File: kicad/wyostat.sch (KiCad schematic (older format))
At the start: 78 parts, among them J1 24 V AC IN, J13 USB_microAB, J16 5V_SEL, J2 OUT1, J3 OUT2, J4 OUT3, J5 I2C_ext1, Q1 BT136-600, Q2 BT136-600, Q3 BT136-600, U1 MOC3063M, U2 MOC3063M, U3 MOC3063M, U4 Wemos-Lolin, U5 MAX17502FATB+T

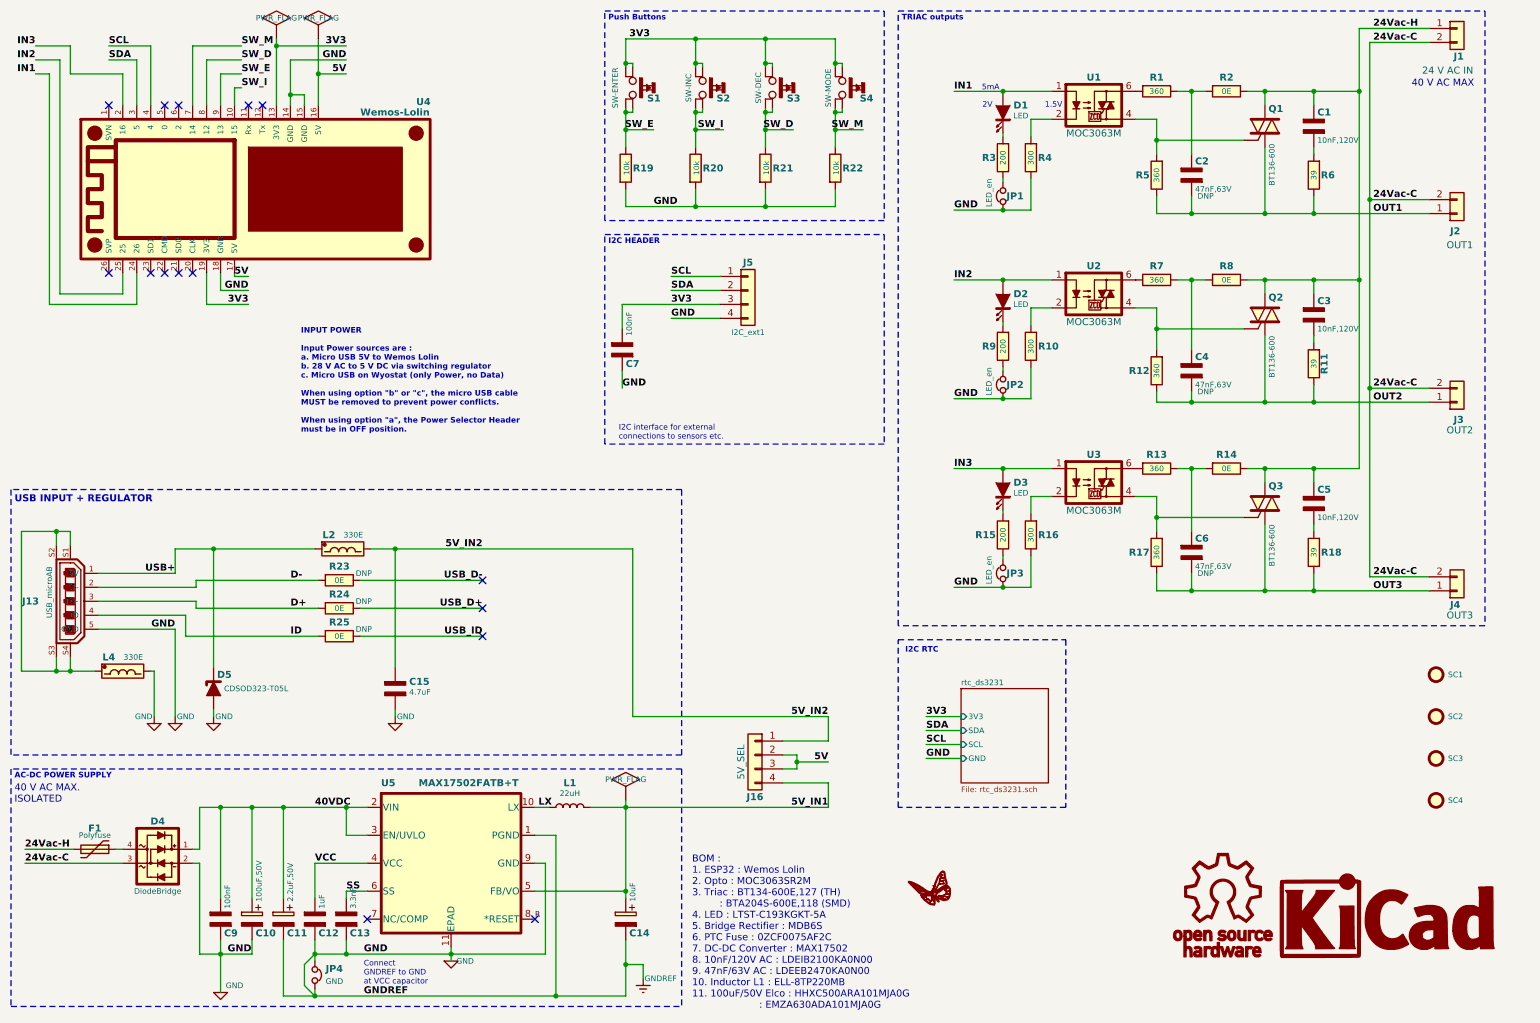
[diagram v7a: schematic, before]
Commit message: Gerbers ready for OSHpark
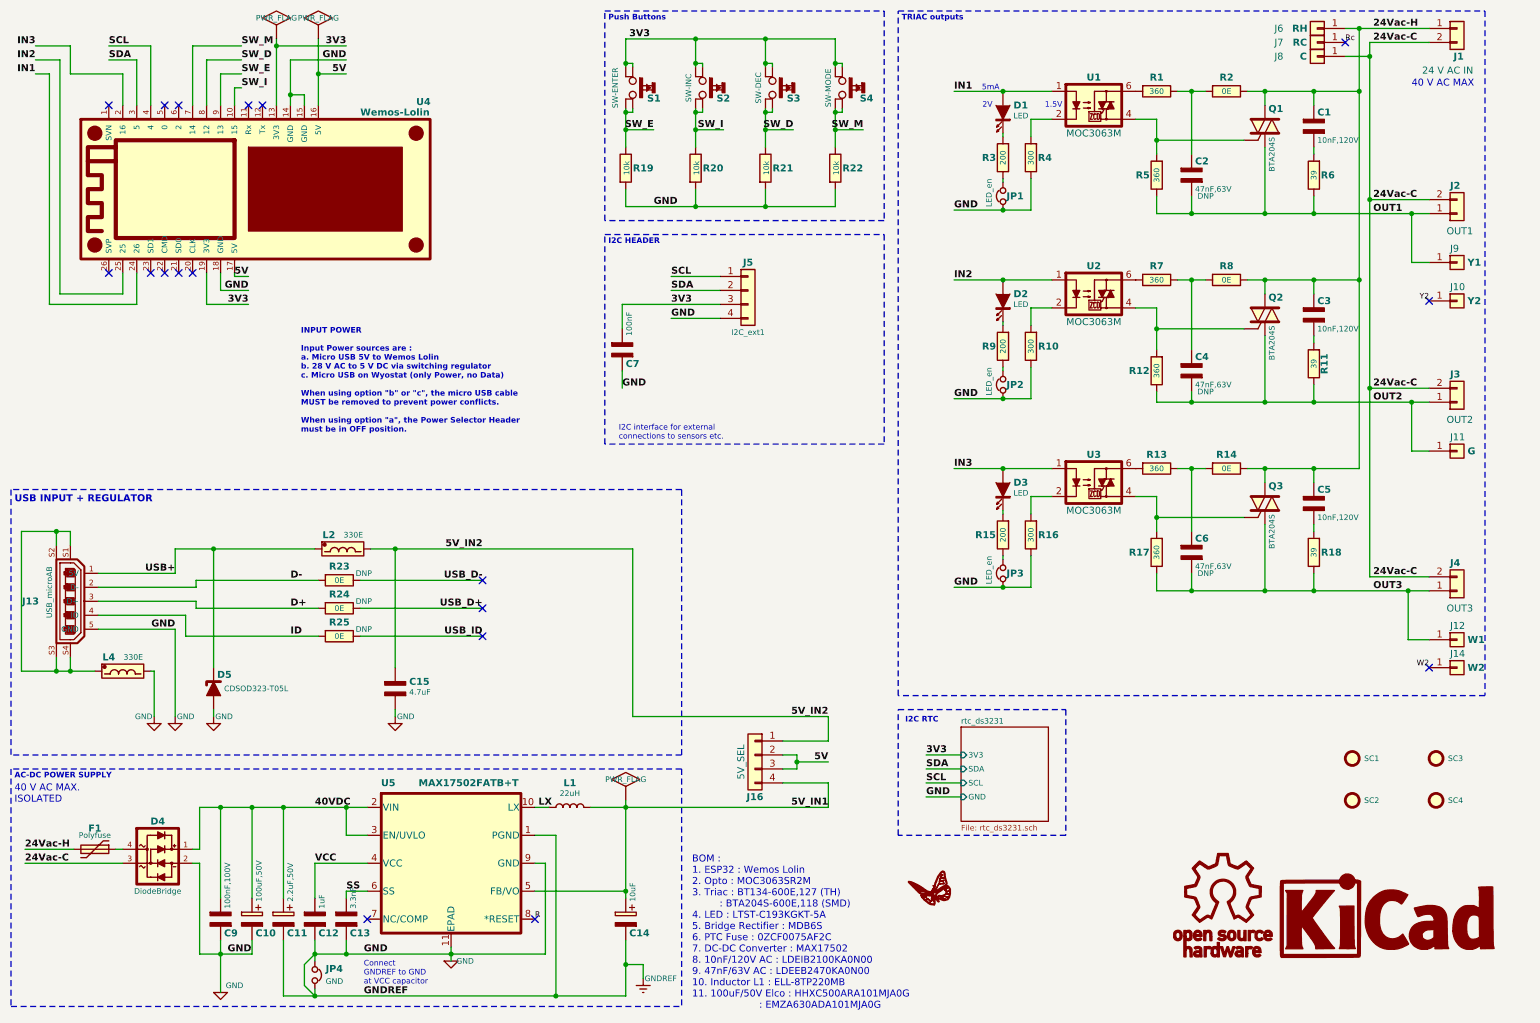
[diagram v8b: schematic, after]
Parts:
- added J10: Y2, wyostat_fp:pad_rect_smd, symbol wyostat:Conn_01x01
- added J11: G, wyostat_fp:pad_rect_smd, symbol wyostat:Conn_01x01
- added J12: W1, wyostat_fp:pad_rect_smd, symbol wyostat:Conn_01x01
- added J14: W2, wyostat_fp:pad_rect_smd, symbol wyostat:Conn_01x01
- added J6: RH, wyostat_fp:pad_rect_smd, symbol wyostat:Conn_01x01
- added J7: RC, wyostat_fp:pad_rect_smd, symbol wyostat:Conn_01x01
- added J8: C, wyostat_fp:pad_rect_smd, symbol wyostat:Conn_01x01
- added J9: Y1, wyostat_fp:pad_rect_smd, symbol wyostat:Conn_01x01
- C1, C2, C3, C4, C5, C6: footprint wyostat_fp:C_2220 -> wyostat_fp:C_1210
- C9: value 100nF -> 100nF,100V; manf# (none) -> mfr_pn
- Q1, Q2, Q3: value BT136-600 -> BTA204S
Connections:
- net 24Vac-C: now also J8.1 (Pin_1)
- net 24Vac-H: now also J6.1 (Pin_1)
- net OUT1: now also J9.1 (Pin_1)
- net OUT2: now also J11.1 (Pin_1)
- net OUT3: now also J12.1 (Pin_1)
- new net Rc: J7.1 (Pin_1)
- new net W2: J14.1 (Pin_1)
- new net Y2: J10.1 (Pin_1)
- no-connect marks 15 -> 18
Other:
- moved on the sheet: SC1, SC2
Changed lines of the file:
@@
 P 9550 1400
 F 0 "Q1" H 9575 1525 50  0000 L CNB
-F 1 "BT136-600" V 9600 975 40  0000 L CNN
+F 1 "BTA204S" V 9600 1075 40  0000 L CNN
 F 2 "wyostat_fp:DPAK-2" H 9750 1325 50  0001 L CIN
 F 3 "" H 9550 1400 50  0000 L CNN
@@
 F 0 "C2" H 9050 1850 50  0000 L CNB
 F 1 "47nF,63V" H 9050 1650 40  0000 L CNN
-F 2 "wyostat_fp:C_2220" H 9025 1750 60  0001 C CNN
+F 2 "wyostat_fp:C_1210" H 9025 1750 60  0001 C CNN
 F 3 "" H 9025 1750 60  0000 C CNN
 F 4 "Value" H 9025 1750 50  0001 C CNN "manf#"
@@
 U 1 1 5AA726AC
 P 10925 2025
-F 0 "J2" H 10875 2150 50  0000 L CNB
-F 1 "OUT1" H 10850 2250 50  0000 L CNN
+F 0 "J2" H 10875 1825 50  0000 L CNB
+F 1 "OUT1" H 10850 2150 50  0000 L CNN
 F 2 "wyostat_fp:TerminalBlock_Pheonix_MPT-2.54mm_2pol" H 10925 2025 50  0001 C CNN
 F 3 "~" H 10925 2025 50  0001 C CNN
@@
 P 9550 2750
 F 0 "Q2" H 9575 2875 50  0000 L CNB
-F 1 "BT136-600" V 9600 2300 40  0000 L CNN
+F 1 "BTA204S" V 9600 2425 40  0000 L CNN
 F 2 "wyostat_fp:DPAK-2" H 9750 2675 50  0001 L CIN
 F 3 "" H 9550 2750 50  0000 L CNN
@@
 U 1 1 5AA791CF
 P 10925 3375
-F 0 "J3" H 10900 3500 50  0000 L CNB
-F 1 "OUT2" H 10850 3575 50  0000 L CNN
+F 0 "J3" H 10875 3175 50  0000 L CNB
+F 1 "OUT2" H 10850 3500 50  0000 L CNN
 F 2 "wyostat_fp:TerminalBlock_Pheonix_MPT-2.54mm_2pol" H 10925 3375 50  0001 C CNN
 F 3 "~" H 10925 3375 50  0001 C CNN
@@
 P 9550 4100
 F 0 "Q3" H 9575 4225 50  0000 L CNB
-F 1 "BT136-600" V 9600 3650 40  0000 L CNN
+F 1 "BTA204S" V 9600 3775 40  0000 L CNN
 F 2 "wyostat_fp:DPAK-2" H 9750 4025 50  0001 L CIN
 F 3 "" H 9550 4100 50  0000 L CNN
@@
 U 1 1 5AA7ACF2
 P 10925 4725
-F 0 "J4" H 10875 4825 50  0000 L CNB
-F 1 "OUT3" H 10850 4900 50  0000 L CNN
+F 0 "J4" H 10875 4525 50  0000 L CNB
+F 1 "OUT3" H 10850 4850 50  0000 L CNN
 F 2 "wyostat_fp:TerminalBlock_Pheonix_MPT-2.54mm_2pol" H 10925 4725 50  0001 C CNN
 F 3 "~" H 10925 4725 50  0001 C CNN
@@
 	6925 575  11125 575
 Wire Notes Line
-	11125 4975 6925 4975
+	11125 5475 6925 5475
 Text Notes 6950 650  0    40   ~ 8
 TRIAC outputs
@@
 P 2075 7075
 F 0 "C9" H 2100 6975 50  0000 L CNB
-F 1 "100nF" V 2125 7150 40  0000 L CNN
+F 1 "100nF,100V" V 2125 7150 40  0000 L CNN
 F 2 "wyostat_fp:C_0805" H 2075 7075 60  0001 C CNN
 F 3 "" H 2075 7075 60  0000 C CNN
+F 4 "mfr_pn" H 2075 7075 50  0001 C CNN "manf#"
 	1    2075 7075
 	1    0    0    -1
@@
 F 0 "C1" H 9925 1500 50  0000 L CNB
 F 1 "10nF,120V" H 9925 1300 40  0000 L CNN
-F 2 "wyostat_fp:C_2220" H 9900 1400 60  0001 C CNN
+F 2 "wyostat_fp:C_1210" H 9900 1400 60  0001 C CNN
 F 3 "" H 9900 1400 60  0000 C CNN
 	1    9900 1400
@@
 F 0 "C3" H 9925 2850 50  0000 L CNB
 F 1 "10nF,120V" H 9925 2650 40  0000 L CNN
-F 2 "wyostat_fp:C_2220" H 9900 2750 60  0001 C CNN
+F 2 "wyostat_fp:C_1210" H 9900 2750 60  0001 C CNN
 F 3 "" H 9900 2750 60  0000 C CNN
 	1    9900 2750
@@
 F 0 "C5" H 9925 4200 50  0000 L CNB
 F 1 "10nF,120V" H 9925 4000 40  0000 L CNN
-F 2 "wyostat_fp:C_2220" H 9900 4100 60  0001 C CNN
+F 2 "wyostat_fp:C_1210" H 9900 4100 60  0001 C CNN
 F 3 "" H 9900 4100 60  0000 C CNN
 	1    9900 4100
@@
 $EndComp
 Wire Notes Line
-	11125 575  11125 4975
+	11125 575  11125 5475
 Wire Notes Line
-	6925 4975 6925 575
+	6925 5475 6925 575
 Wire Wire Line
 	3725 7325 2975 7325
@@
 	10725 700  10225 700
 Wire Wire Line
-	10300 800  10300 1925
+	10300 800  10300 900
 Wire Wire Line
 	10300 800  10725 800
@@
 Connection ~ 10300 3275
 Wire Wire Line
-	9900 2025 10725 2025
+	9900 2025 10600 2025
 Wire Wire Line
-	9900 3375 10725 3375
+	9900 3375 10600 3375
 Wire Wire Line
-	9900 4725 10725 4725
+	9900 4725 10575 4725
 Wire Wire Line
 	9900 1150 10225 1150
@@
 L wyostat:SCREW SC1
 U 1 1 5AED1CEA
-P 10775 5325
-F 0 "SC1" H 10860 5325 40  0000 L CNN
-F 1 "SCREW" H 10775 5425 40  0001 C CNN
-F 2 "wyostat_fp:MountingHole_3.2mm_M3_Pad_Via" H 10775 5325 60  0001 C CNN
-F 3 "" H 10775 5325 60  0000 C CNN
-	1    10775 5325
+P 10175 5925
+F 0 "SC1" H 10260 5925 40  0000 L CNN
+F 1 "SCREW" H 10175 6025 40  0001 C CNN
+F 2 "wyostat_fp:MountingHole_3.2mm_M3_Pad_Via" H 10175 5925 60  0001 C CNN
+F 3 "" H 10175 5925 60  0000 C CNN
+	1    10175 5925
 	1    0    0    -1
 $EndComp
@@
 L wyostat:SCREW SC2
 U 1 1 5AED2014
-P 10775 5625
-F 0 "SC2" H 10860 5625 40  0000 L CNN
-F 1 "SCREW" H 10775 5725 40  0001 C CNN
-F 2 "wyostat_fp:MountingHole_3.2mm_M3_Pad_Via" H 10775 5625 60  0001 C CNN
-F 3 "" H 10775 5625 60  0000 C CNN
-	1    10775 5625
+P 10175 6225
+F 0 "SC2" H 10260 6225 40  0000 L CNN
+F 1 "SCREW" H 10175 6325 40  0001 C CNN
+F 2 "wyostat_fp:MountingHole_3.2mm_M3_Pad_Via" H 10175 6225 60  0001 C CNN
+F 3 "" H 10175 6225 60  0000 C CNN
+	1    10175 6225
 	1    0    0    -1
 $EndComp
@@
 F 0 "C4" H 9050 3250 50  0000 L CNB
 F 1 "47nF,63V" H 9050 3050 40  0000 L CNN
-F 2 "wyostat_fp:C_2220" H 9025 3150 60  0001 C CNN
+F 2 "wyostat_fp:C_1210" H 9025 3150 60  0001 C CNN
 F 3 "" H 9025 3150 60  0000 C CNN
 F 4 "Value" H 9025 3150 50  0001 C CNN "manf#"
@@
 F 0 "C6" H 9050 4550 50  0000 L CNB
 F 1 "47nF,63V" H 9050 4350 40  0000 L CNN
-F 2 "wyostat_fp:C_2220" H 9025 4450 60  0001 C CNN
+F 2 "wyostat_fp:C_1210" H 9025 4450 60  0001 C CNN
 F 3 "" H 9025 4450 60  0000 C CNN
 F 4 "Value" H 9025 4450 50  0001 C CNN "manf#"
@@
 	3325 4425 5025 4425
 $Sheet
-S 7375 5425 625  675
+S 7375 5700 625  675
 U 5AE47A99
 F0 "rtc_ds3231" 40
 F1 "rtc_ds3231.sch" 40
-F2 "3V3" I L 7375 5625 40
-F3 "GND" I L 7375 5925 40
-F4 "SDA" I L 7375 5725 40
-F5 "SCL" I L 7375 5825 40
+F2 "3V3" I L 7375 5900 40
+F3 "GND" I L 7375 6200 40
+F4 "SDA" I L 7375 6000 40
+F5 "SCL" I L 7375 6100 40
 $EndSheet
 Wire Wire Line
-	7375 5625 7125 5625
+	7375 5900 7125 5900
 Wire Wire Line
-	7125 5725 7375 5725
+	7125 6000 7375 6000
 Wire Wire Line
-	7375 5825 7125 5825
+	7375 6100 7125 6100
 Wire Wire Line
-	7125 5925 7375 5925
-Text Label 7125 5925 0    50   ~ 10
+	7125 6200 7375 6200
+Text Label 7125 6200 0    50   ~ 10
 GND
-Text Label 7125 5625 0    50   ~ 10
+Text Label 7125 5900 0    50   ~ 10
 3V3
-Text Label 7125 5825 0    50   ~ 10
+Text Label 7125 6100 0    50   ~ 10
 SCL
-Text Label 7125 5725 0    50   ~ 10
+Text Label 7125 6000 0    50   ~ 10
 SDA
 Wire Notes Line
-	8125 5075 8125 6275
+	8125 5575 8125 6475
 Wire Notes Line
-	8125 6275 6925 6275
+	8125 6475 6925 6475
 Wire Notes Line
-	6925 6275 6925 5075
+	6925 6475 6925 5575
 Wire Notes Line
-	6925 5075 8125 5075
-Text Notes 6975 5175 0    40   ~ 8
+	6925 5575 8125 5575
+Text Notes 6975 5675 0    40   ~ 8
 I2C RTC
 $Comp
@@
 	1    0    0    -1
 $EndComp
+$Comp
+L wyostat:Conn_01x01 J6
+U 1 1 5AB1854D
+P 9925 700
+F 0 "J6" H 10200 700 50  0000 C CNN
+F 1 "RH" H 10050 700 50  0000 C CNB
+F 2 "wyostat_fp:pad_rect_smd" H 9925 700 50  0001 C CNN
+F 3 "" H 9925 700 50  0001 C CNN
+	1    9925 700
+	-1   0    0    1
+$EndComp
+$Comp
+L wyostat:Conn_01x01 J7
+U 1 1 5AB186B9
+P 9925 800
+F 0 "J7" H 10200 800 50  0000 C CNN
+F 1 "RC" H 10050 800 50  0000 C CNB
+F 2 "wyostat_fp:pad_rect_smd" H 9925 800 50  0001 C CNN
+F 3 "" H 9925 800 50  0001 C CNN
+	1    9925 800
+	-1   0    0    1
+$EndComp
+$Comp
+L wyostat:Conn_01x01 J8
+U 1 1 5AB18767
+P 9925 900
+F 0 "J8" H 10200 900 50  0000 C CNN
+F 1 "C" H 10025 900 50  0000 C CNB
+F 2 "wyostat_fp:pad_rect_smd" H 9925 900 50  0001 C CNN
+F 3 "" H 9925 900 50  0001 C CNN
+	1    9925 900
+	-1   0    0    1
+$EndComp
+Wire Wire Line
+	10225 700  10125 700
+Connection ~ 10225 700
+Wire Wire Line
+	10125 900  10300 900
+Connection ~ 10300 900
+Wire Wire Line
+	10300 900  10300 1925
+NoConn ~ 10125 800
+$Comp
+L wyostat:Conn_01x01 J11
+U 1 1 5AB8BFF5
+P 10925 3725
+F 0 "J11" H 10875 3825 50  0000 L CNN
+F 1 "G" H 11000 3725 50  0000 L CNB
+F 2 "wyostat_fp:pad_rect_smd" H 10925 3725 50  0001 C CNN
+F 3 "" H 10925 3725 50  0001 C CNN
+	1    10925 3725
+	1    0    0    -1
+$EndComp
+Wire Wire Line
+	10725 3725 10600 3725
+Wire Wire Line
+	10600 3725 10600 3375
+Connection ~ 10600 3375
+Wire Wire Line
+	10600 3375 10725 3375
+$Comp
+L wyostat:Conn_01x01 J9
+U 1 1 5ABA94CF
+P 10925 2375
+F 0 "J9" H 10875 2475 50  0000 L CNN
+F 1 "Y1" H 11000 2375 50  0000 L CNB
+F 2 "wyostat_fp:pad_rect_smd" H 10925 2375 50  0001 C CNN
+F 3 "" H 10925 2375 50  0001 C CNN
+	1    10925 2375
+	1    0    0    -1
+$EndComp
+$Comp
+L wyostat:Conn_01x01 J10
+U 1 1 5ABA96DB
+P 10925 2650
+F 0 "J10" H 10875 2750 50  0000 L CNN
+F 1 "Y2" H 11000 2650 50  0000 L CNB
+F 2 "wyostat_fp:pad_rect_smd" H 10925 2650 50  0001 C CNN
+F 3 "" H 10925 2650 50  0001 C CNN
+	1    10925 2650
+	1    0    0    -1
+$EndComp
+NoConn ~ 10725 2650
+Wire Wire Line
+	10725 2375 10600 2375
+Wire Wire Line
+	10600 2375 10600 2025
+Connection ~ 10600 2025
+Wire Wire Line
+	10600 2025 10725 2025
+$Comp
+L wyostat:Conn_01x01 J12
+U 1 1 5AD0DEA5
+P 10925 5075
+F 0 "J12" H 10875 5175 50  0000 L CNN
+F 1 "W1" H 11000 5075 50  0000 L CNB
+F 2 "wyostat_fp:pad_rect_smd" H 10925 5075 50  0001 C CNN
+F 3 "" H 10925 5075 50  0001 C CNN
+	1    10925 5075
+	1    0    0    -1
+$EndComp
+$Comp
+L wyostat:Conn_01x01 J14
+U 1 1 5AD0E58F
+P 10925 5275
+F 0 "J14" H 10875 5375 50  0000 L CNN
+F 1 "W2" H 11000 5275 50  0000 L CNB
+F 2 "wyostat_fp:pad_rect_smd" H 10925 5275 50  0001 C CNN
+F 3 "" H 10925 5275 50  0001 C CNN
+	1    10925 5275
+	1    0    0    -1
+$EndComp
+NoConn ~ 10725 5275
+Wire Wire Line
+	10725 5075 10575 5075
+Wire Wire Line
+	10575 5075 10575 4725
+Connection ~ 10575 4725
+Wire Wire Line
+	10575 4725 10725 4725
+Text Label 10725 2650 2    40   ~ 0
+Y2
+Text Label 10725 5275 2    40   ~ 0
+W2
+Text Label 10125 800  0    40   ~ 0
+Rc
 $EndSCHEMATC
